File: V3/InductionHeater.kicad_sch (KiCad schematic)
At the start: 133 parts, among them Q1 2N2219, Q2 PNP, Q3 PNP, Q4 2N2219, Q5 FF200R12KS4, Q6 FF200R12KS4, Q7 FF200R12KS4, Q8 FF200R12KS4, SW1 SW_DPDT_x2, SW2 Freq_up_pushBtn, SW3 Freq_down_pushBtn, SW4 SW_DPDT_x2 (Freq. Lock), SW5 SW_DPDT_x2 (PWM Enable), SW6 5V Relay, U1 STM32F103C8Tx, U3 LM339

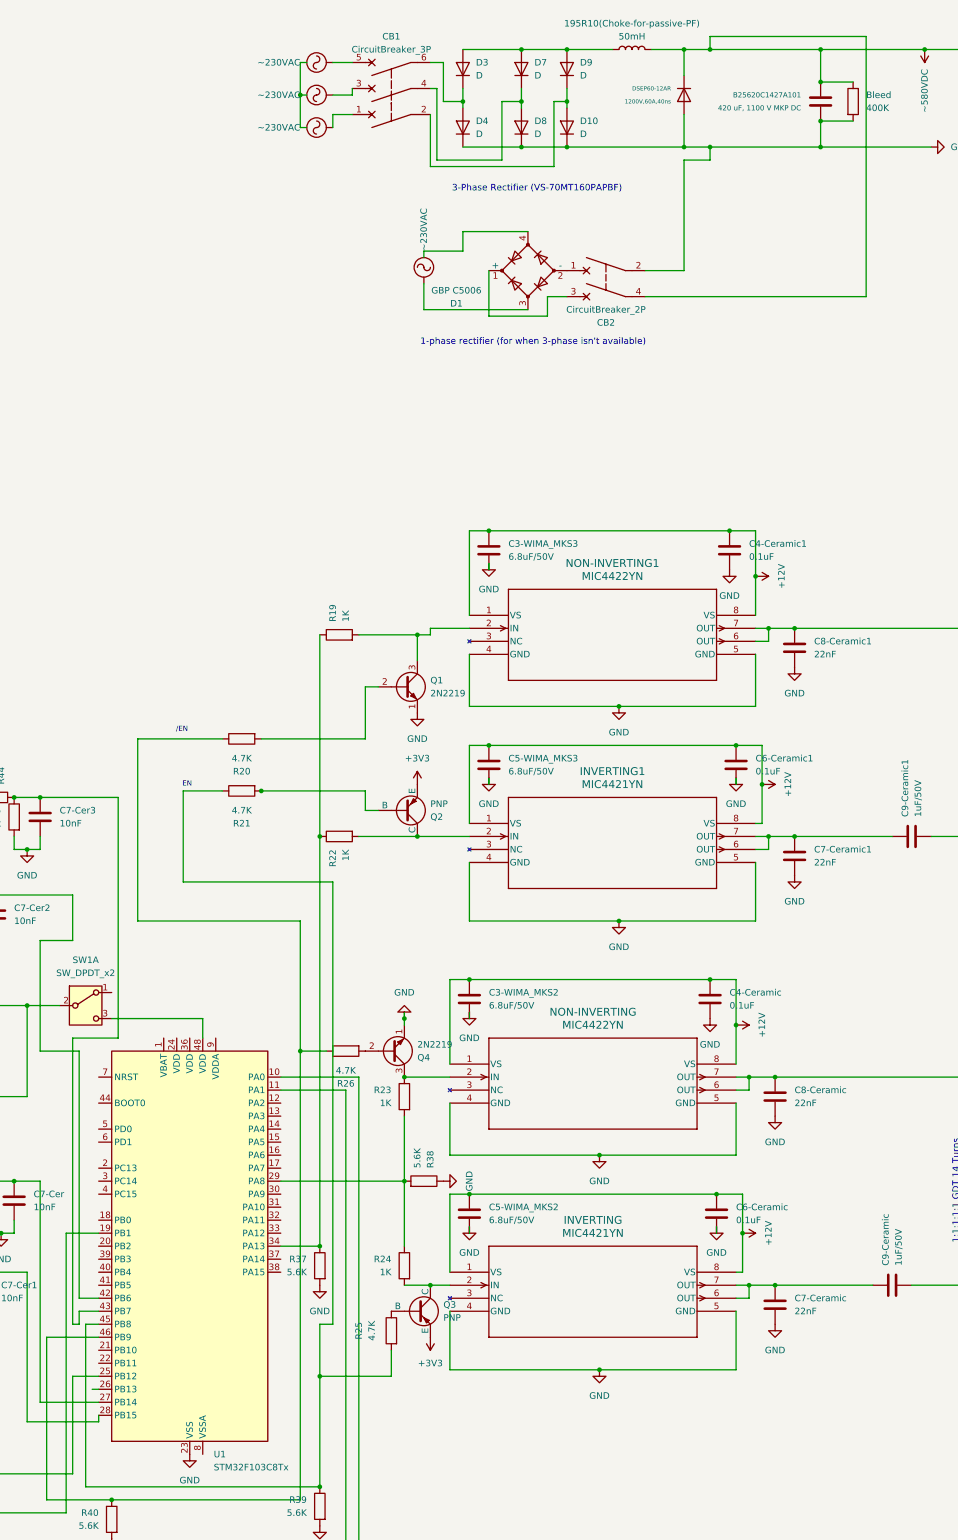
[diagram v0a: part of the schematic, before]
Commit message: V3 schematic: add passive PFC choke and bulk cap, refresh PDF
Schematic changes:
- Add 5mH choke 195G10 for passive PFC
- Add C2, 3mF bulk electrolytic
- Fix reference typo on the existing choke:
  195R10(Choke-for-passive-PF) -> 195R10(Choke-for-passive-PFC)

Re-plotted InductionHeater.pdf from the schematic with kicad-cli 10.0.4
(sch export pdf) so the exported view matches the source again.

Co-Authored-By: Claude Opus 5 <noreply@anthropic.com>
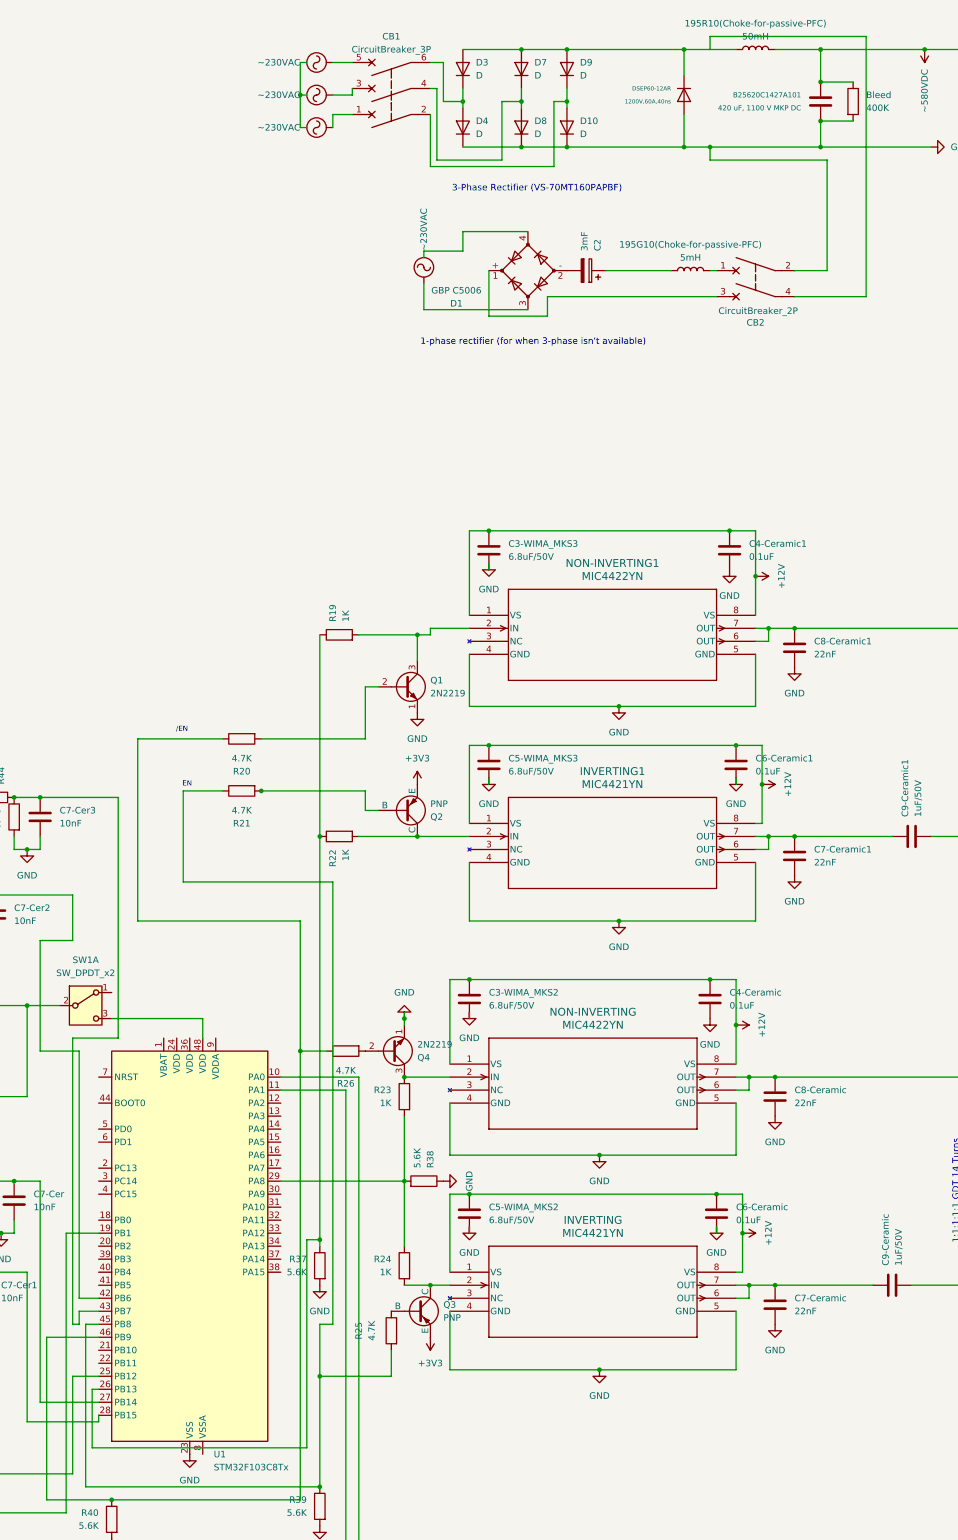
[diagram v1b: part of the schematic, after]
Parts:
- added 195G10(Choke-for-passive-PFC): 5mH, symbol Device:L
- added C2: 3mF, symbol Device:C_Polarized
- renumbered 195R10(Choke-for-passive-PF) to 195R10(Choke-for-passive-PFC)
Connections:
- net ~580VDC: no longer CB2.4, DSEP60-12AR.1 (K)
- net at 195R10(Choke-for-passive-PFC).1, D3.2 (A), D7.2 (A)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: now also DSEP60-12AR.1 (K)
- net at R19.1, R22.1, R37.1: now also U1.26 (PB13); no longer U1.34 (PA13)
- net at D1.2 (-): now also C2.2; no longer CB2.1
- new net: 195G10(Choke-for-passive-PFC).1, C2.1
- new net: 195G10(Choke-for-passive-PFC).2, CB2.1
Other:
- moved on the sheet: 195R10(Choke-for-passive-PFC), CB2

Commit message: V3 schematic: fix GDT ratio label, mirror gate-drive symbols
- Correct the gate drive transformer annotation from
  "1:1:1:1:1 GDT 14 Turns" to "1:1:1 GDT 14 Turns" (both instances)
- Mirror six symbols in the gate-drive area (x = 157.48 / 168.91 /
  177.8), flipping their pin and property placement to match

No components added or removed; netlist is unchanged.

Re-plotted InductionHeater.pdf with kicad-cli 10.0.4 (sch export pdf).

Co-Authored-By: Claude Opus 5 <noreply@anthropic.com>
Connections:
- net GND: now also D10.2 (A), D4.2 (A), D8.2 (A); no longer D10.1 (K), D4.1 (K), D8.1 (K)
- new net: 195R10(Choke-for-passive-PFC).1, D3.1 (K), D7.1 (K), D9.1 (K), DSEP60-12AR.1 (K)
- new net: CB1.6, D3.2 (A), D4.1 (K)
- new net: CB1.2, D10.1 (K), D9.2 (A)
- new net: CB1.4, D7.2 (A), D8.1 (K)
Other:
- note added: "1:1:1 GDT 14 Turns"
- note removed: "1:1:1:1:1 GDT 14 Turns"
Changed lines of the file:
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@@
 		)
 	)
-	(text "1:1:1:1:1 GDT 14 Turns "
+	(text "1:1:1 GDT 14 Turns "
 		(exclude_from_sim no)
 		(at 255.016 160.782 90)
@@
 		)
 	)
-	(text "1:1:1:1:1 GDT 14 Turns "
+	(text "1:1:1 GDT 14 Turns "
 		(exclude_from_sim no)
 		(at 251.206 248.412 90)
@@
 		(lib_id "Device:D")
 		(at 154.94 29.21 90)
+		(mirror x)
 		(unit 1)
 		(body_style 1)
@@
 		(fields_autoplaced yes)
 		(property "Reference" "D3"
-			(at 157.48 27.9399 90)
+			(at 157.48 30.4801 90)
 			(show_name no)
 			(do_not_autoplace no)
@@
 		)
 		(property "Value" "D"
-			(at 157.48 30.4799 90)
+			(at 157.48 27.9401 90)
 			(show_name no)
 			(do_not_autoplace no)
@@
 		(lib_id "Device:D")
 		(at 175.26 40.64 90)
+		(mirror x)
 		(unit 1)
 		(body_style 1)
@@
 		(fields_autoplaced yes)
 		(property "Reference" "D10"
-			(at 177.8 39.3699 90)
+			(at 177.8 41.9101 90)
 			(show_name no)
 			(do_not_autoplace no)
@@
 		)
 		(property "Value" "D"
-			(at 177.8 41.9099 90)
+			(at 177.8 39.3701 90)
 			(show_name no)
 			(do_not_autoplace no)
@@
 		(lib_id "Device:D")
 		(at 175.26 29.21 90)
+		(mirror x)
 		(unit 1)
 		(body_style 1)
@@
 		(fields_autoplaced yes)
 		(property "Reference" "D9"
-			(at 177.8 27.9399 90)
+			(at 177.8 30.4801 90)
 			(show_name no)
 			(do_not_autoplace no)
@@
 		)
 		(property "Value" "D"
-			(at 177.8 30.4799 90)
+			(at 177.8 27.9401 90)
 			(show_name no)
 			(do_not_autoplace no)
@@
 		(lib_id "Device:D")
 		(at 154.94 40.64 90)
+		(mirror x)
 		(unit 1)
 		(body_style 1)
@@
 		(fields_autoplaced yes)
 		(property "Reference" "D4"
-			(at 157.48 39.3699 90)
+			(at 157.48 41.9101 90)
 			(show_name no)
 			(do_not_autoplace no)
@@
 		)
 		(property "Value" "D"
-			(at 157.48 41.9099 90)
+			(at 157.48 39.3701 90)
 			(show_name no)
 			(do_not_autoplace no)
@@
 		(lib_id "Device:D")
 		(at 166.37 29.21 90)
+		(mirror x)
 		(unit 1)
 		(body_style 1)
@@
 		(fields_autoplaced yes)
 		(property "Reference" "D7"
-			(at 168.91 27.9399 90)
+			(at 168.91 30.4801 90)
 			(show_name no)
 			(do_not_autoplace no)
@@
 		)
 		(property "Value" "D"
-			(at 168.91 30.4799 90)
+			(at 168.91 27.9401 90)
 			(show_name no)
 			(do_not_autoplace no)
@@
 		(lib_id "Device:D")
 		(at 166.37 40.64 90)
+		(mirror x)
 		(unit 1)
 		(body_style 1)
@@
 		(fields_autoplaced yes)
 		(property "Reference" "D8"
-			(at 168.91 39.3699 90)
+			(at 168.91 41.9101 90)
 			(show_name no)
 			(do_not_autoplace no)
@@
 		)
 		(property "Value" "D"
-			(at 168.91 41.9099 90)
+			(at 168.91 39.3701 90)
 			(show_name no)
 			(do_not_autoplace no)

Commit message: V3 schematic: add run-timer pot, fix C2 placement, add soft-charge input
- Add RV1 (10k) for the run-timer setpoint: ends on +3V3/GND, wiper
  to PA2 (U1 pin 12) via the POT_WIPER net label. Placed beside the
  OLED power hookup.
- Move C2 (3mF) from series in the rectifier's negative leg to across
  the single-phase DC output, after the passive-PFC choke and before
  CB2, so it is isolated from the 580VDC bus when CB2 is open.
- Add single-pole main breaker CB4 in the Line feed to the single-phase
  bridge, with a parallel soft-charge branch (CB5 + halogen lamp LA1)
  to precharge the capacitors before closing CB4.
- Connect the bridge's second AC input (D1 pin 4) to NEUT; it was
  previously unconnected.
- Move labels so none overlap text or wires in the edited areas.

Re-plotted InductionHeater.pdf with kicad-cli 10.0.4.

Co-Authored-By: Claude Opus 5.5 <noreply@anthropic.com>
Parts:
- added CB4: Main 1P, symbol Device:CircuitBreaker_1P
- added CB5: Soft-charge 1P, symbol Device:CircuitBreaker_1P
- added LA1: Halogen (precharge R), symbol Device:Lamp
- added RV1: 10k, symbol Device:R_Potentiometer
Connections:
- net +3V3: now also RV1.1
- net GND: now also RV1.3
- net ~230VAC: now also CB4.1, CB5.1; no longer D1.3
- net at C2.1: now also CB2.3, D1.1 (+); no longer 195G10(Choke-for-passive-PFC).1
- net at C2.2: now also 195G10(Choke-for-passive-PFC).2, CB2.1; no longer D1.2 (-)
- net POT_WIPER: now reaches U1.12 (PA2)
- net POT_WIPER: now also RV1.2
- net NEUT: now reaches D1.4
- new net: CB4.2, D1.3, LA1.1 (-)
- new net: CB5.2, LA1.2 (+)
- new net: 195G10(Choke-for-passive-PFC).1, D1.2 (-)
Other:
- moved on the sheet: 195G10(Choke-for-passive-PFC), C2

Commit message: V3 schematic: move C2 directly across the single-phase bridge
Place C2 (3mF) across D1's DC output, before the passive-PFC choke,
matching the wiring drawn in the working KiCad project. The choke
returns to its original position between D1(-) and CB2.

Re-plotted InductionHeater.pdf with kicad-cli 10.0.4.

Co-Authored-By: Claude Opus 5.5 <noreply@anthropic.com>
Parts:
- C2: value 3mF -> 3mF, 400V
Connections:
- net at 195G10(Choke-for-passive-PFC).2, CB2.1: no longer C2.2
- net at 195G10(Choke-for-passive-PFC).1, D1.2 (-): now also C2.2
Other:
- moved on the sheet: 195G10(Choke-for-passive-PFC), C2
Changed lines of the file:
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@@
 		(color 0 0 0 0)
 	)
-	(junction
-		(at 345.44 176.53)
-		(diameter 0)
-		(color 0 0 0 0)
-	)
 	(wire
 		(pts
@@
 	(symbol
 		(lib_id "Device:C_Polarized")
-		(at 196.85 72.39 180)
+		(at 179.07 72.39 0)
+		(mirror x)
 		(unit 1)
 		(body_style 1)
@@
 		(in_pos_files yes)
 		(dnp no)
+		(fields_autoplaced yes)
 		(property "Reference" "C2"
-			(at 193.04 71.12 0)
+			(at 182.88 74.5491 0)
 			(show_name no)
 			(do_not_autoplace no)
@@
 			)
 		)
-		(property "Value" "3mF"
-			(at 193.04 73.66 0)
+		(property "Value" "3mF, 400V"
+			(at 182.88 72.0091 0)
 			(show_name no)
 			(do_not_autoplace no)
@@
 		)
 		(property "Footprint" ""
-			(at 175.26 67.6148 0)
+			(at 180.0352 68.58 0)
 			(hide yes)
 			(show_name no)
@@
 		)
 		(property "Datasheet" ""
-			(at 179.07 68.58 0)
+			(at 179.07 72.39 0)
 			(hide yes)
 			(show_name no)
@@
 		)
 		(property "Description" "Polarized capacitor"
-			(at 179.07 68.58 0)
+			(at 179.07 72.39 0)
 			(hide yes)
 			(show_name no)
@@
 	(symbol
 		(lib_id "Device:L")
-		(at 186.69 68.58 90)
+		(at 199.39 68.58 90)
 		(unit 1)
 		(body_style 1)
@@
 		(fields_autoplaced yes)
 		(property "Reference" "195G10(Choke-for-passive-PFC)"
-			(at 186.69 63.5 90)
+			(at 199.39 63.5 90)
 			(show_name no)
 			(do_not_autoplace no)
@@
 		)
 		(property "Value" "5mH"
-			(at 186.69 66.04 90)
+			(at 199.39 66.04 90)
 			(show_name no)
 			(do_not_autoplace no)
@@
 		)
 		(property "Footprint" ""
-			(at 186.69 68.58 0)
+			(at 199.39 68.58 0)
 			(hide yes)
 			(show_name no)
@@
 		)
 		(property "Datasheet" ""
-			(at 186.69 68.58 0)
+			(at 199.39 68.58 0)
 			(hide yes)
 			(show_name no)
@@
 		)
 		(property "Description" "Inductor"
-			(at 186.69 68.58 0)
+			(at 199.39 68.58 0)
 			(hide yes)
 			(show_name no)
@@
 	(wire
 		(pts
-			(xy 175.26 68.58) (xy 182.88 68.58)
-		)
-		(stroke
-			(width 0)
-			(type default)
-		)
-	)
-	(wire
-		(pts
-			(xy 190.5 68.58) (xy 196.85 68.58)
-		)
-		(stroke
-			(width 0)
-			(type default)
-		)
-	)
-	(wire
-		(pts
-			(xy 196.85 68.58) (xy 204.47 68.58)
-		)
-		(stroke
-			(width 0)
-			(type default)
-		)
-	)
-	(wire
-		(pts
-			(xy 160.02 77.47) (xy 196.85 77.47)
-		)
-		(stroke
-			(width 0)
-			(type default)
-		)
-	)
-	(wire
-		(pts
-			(xy 196.85 77.47) (xy 204.47 77.47)
-		)
-		(stroke
-			(width 0)
-			(type default)
-		)
-	)
-	(wire
-		(pts
 			(xy 204.47 77.47) (xy 204.47 73.66)
 		)
@@
 		)
 	)
-	(wire
-		(pts
-			(xy 196.85 76.2) (xy 196.85 77.47)
-		)
-		(stroke
-			(width 0)
-			(type default)
-		)
-	)
-	(junction
-		(at 196.85 68.58)
-		(diameter 0)
-		(color 0 0 0 0)
-	)
 	(junction
 		(at 196.85 77.47)
@@
 		)
 	)
+	(wire
+		(pts
+			(xy 175.26 68.58) (xy 179.07 68.58)
+		)
+		(stroke
+			(width 0)
+			(type default)
+		)
+	)
+	(wire
+		(pts
+			(xy 179.07 68.58) (xy 195.58 68.58)
+		)
+		(stroke
+			(width 0)
+			(type default)
+		)
+	)
+	(junction
+		(at 179.07 68.58)
+		(diameter 0)
+		(color 0 0 0 0)
+	)
+	(wire
+		(pts
+			(xy 203.2 68.58) (xy 204.47 68.58)
+		)
+		(stroke
+			(width 0)
+			(type default)
+		)
+	)
+	(wire
+		(pts
+			(xy 160.02 77.47) (xy 179.07 77.47)
+		)
+		(stroke
+			(width 0)
+			(type default)
+		)
+	)
+	(wire
+		(pts
+			(xy 179.07 77.47) (xy 204.47 77.47)
+		)
+		(stroke
+			(width 0)
+			(type default)
+		)
+	)
+	(junction
+		(at 179.07 77.47)
+		(diameter 0)
+		(color 0 0 0 0)
+	)
+	(wire
+		(pts
+			(xy 179.07 76.2) (xy 179.07 77.47)
+		)
+		(stroke
+			(width 0)
+			(type default)
+		)
+	)
